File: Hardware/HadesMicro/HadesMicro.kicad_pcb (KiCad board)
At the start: 4 copper layers, 40 x 40 mm, 86 parts

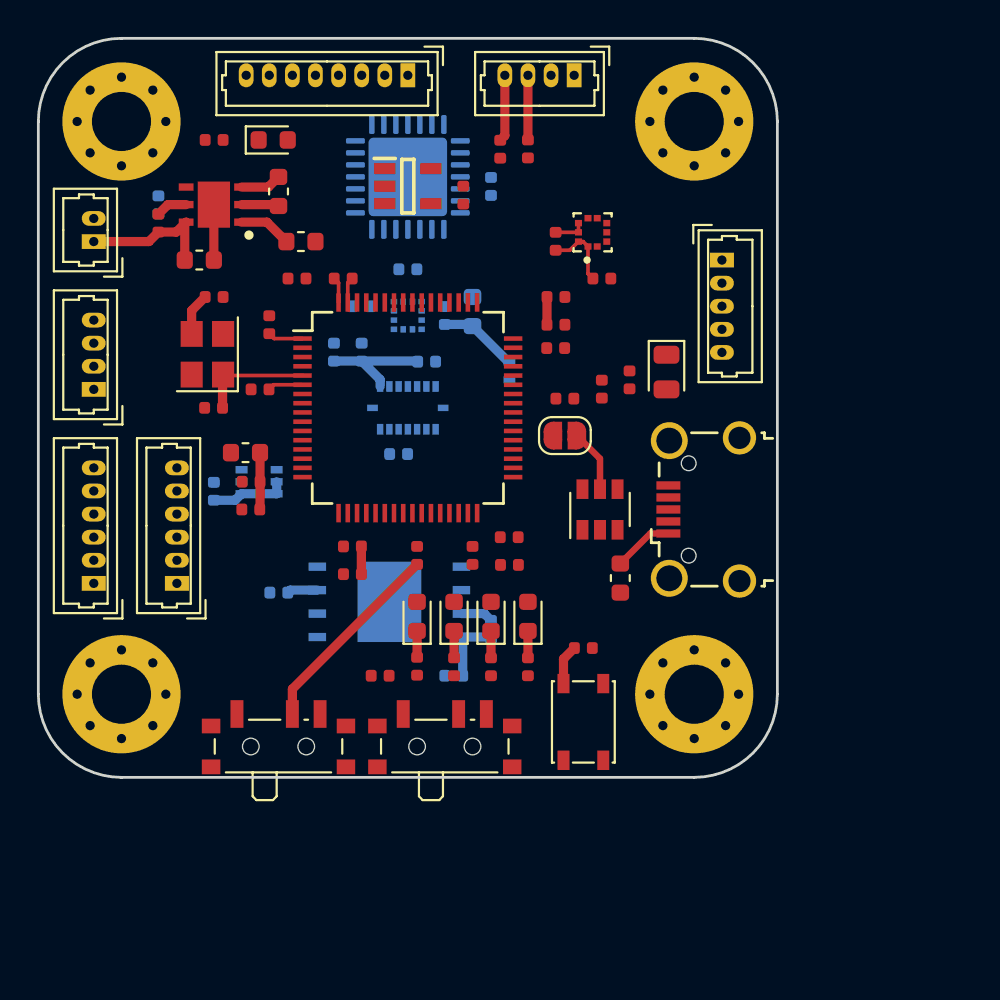
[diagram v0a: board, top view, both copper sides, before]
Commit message: Added TMP100 driver.
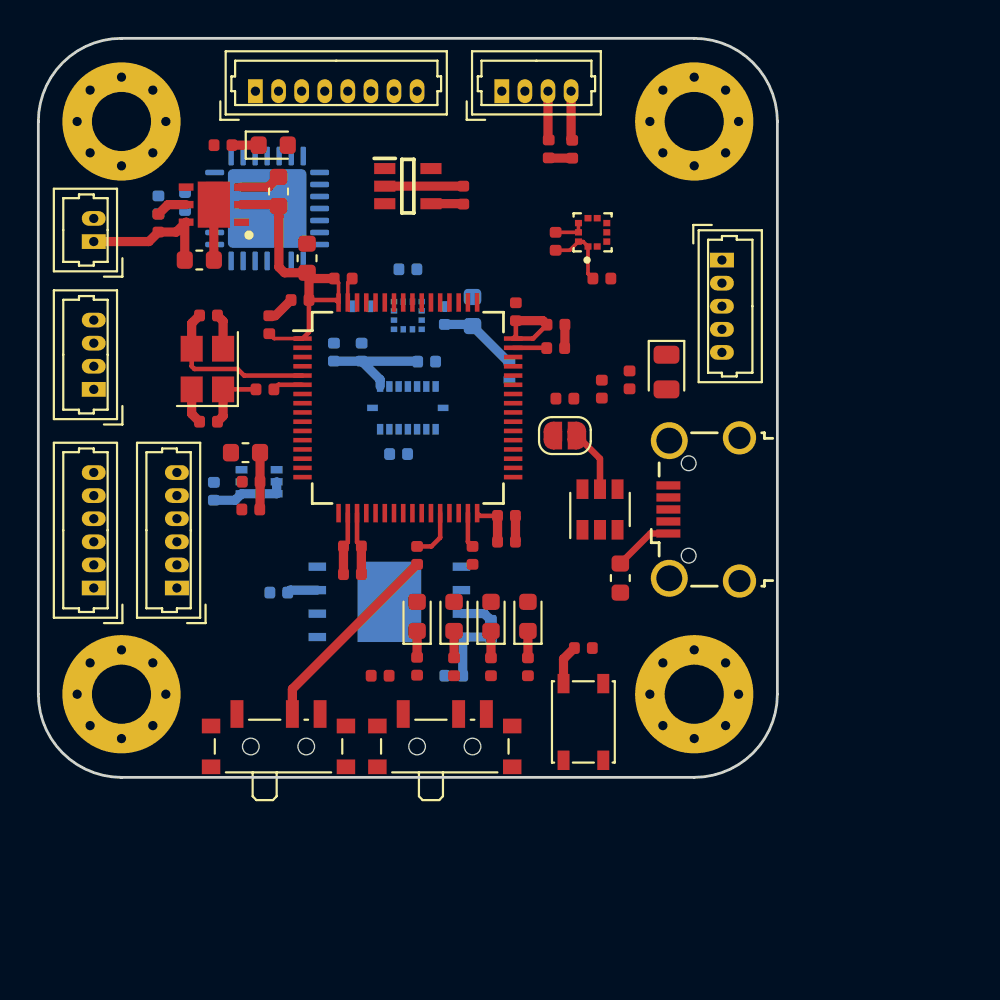
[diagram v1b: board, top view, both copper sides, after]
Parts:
- moved ? 16.6 mm to (27.9, 28.8), turned to 90 degrees
- moved ? 8.29 mm to (31.8, 22.9), turned to 0 degrees
- moved ? 7.80 mm to (32.4, 29.2), turned to 270 degrees
- moved ? 6.76 mm to (29.2, 40.8), turned to 180 degrees
- moved ? 5.01 mm to (29.2, 35.0), turned to 0 degrees
- moved ? 4.01 mm to (45.1, 22.9), turned to 0 degrees
- moved ? 3.90 mm to (48.9, 26.0)
- moved ? 2.31 mm to (45.8, 34.8), turned to 90 degrees
- moved ? 1.27 mm to (45.3, 47.2)
- moved ? 1.17 mm to (34.2, 34.2), turned to 180 degrees
- moved ? 1.16 mm to (45.3, 45.8)
- moved ? 1.12 mm to (47.6, 26.0)
- moved ? 0.96 mm to (34.5, 31.9), turned to 90 degrees
- moved ? 0.80 mm to (29.1, 37.9)
- moved ? 0.56 mm to (30.0, 25.8)
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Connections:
- ? pad 1: HSE_IN -> Net-(C18-Pad1)
- ? pad 3: Net-(C18-Pad1) -> HSE_IN
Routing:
- net +3V3: track 33.7 -> 54.1 mm
- net GND: track 8.36 -> 24.1 mm
- net HSE_IN: track 6.13 -> 9.13 mm
- net BOOT1: track 0.00 -> 2.77 mm
- net Net-(C13-Pad1): track 0.00 -> 1.90 mm
- net Net-(C14-Pad1): track 0.00 -> 1.82 mm
- net Net-(PWR1-Pad1): track 0.00 -> 1.45 mm
- net Net-(C18-Pad1): track 2.30 -> 3.68 mm
- net I2C3_SDA: track 3.62 -> 2.68 mm
- net I2C3_SCL: track 3.50 -> 2.66 mm

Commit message: Completed HadesMicro PCB. SWD works on F4.
- Finalised board. Added Gerbers and assembly files.
- Tested SWD via ST-LINK adapter and STM32F4 (NAVC). Debug works flawlessly in STM32CubeIDE.
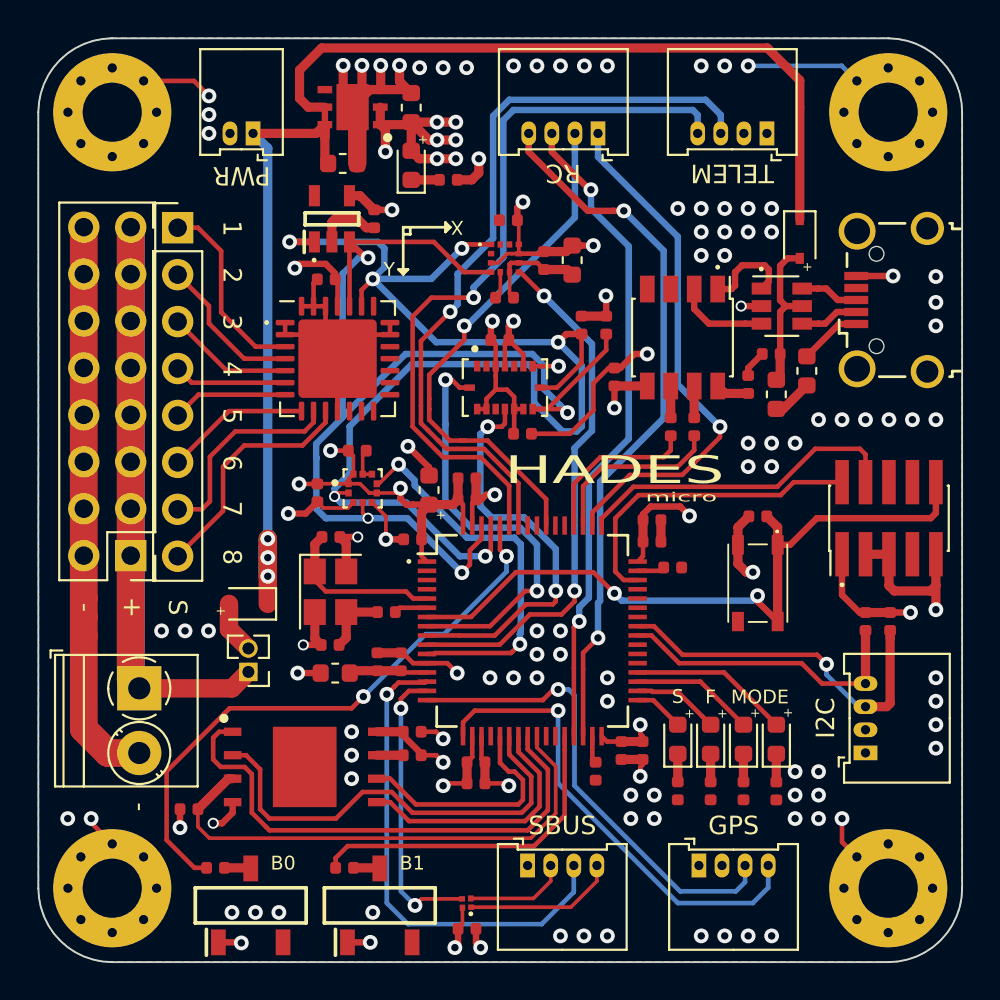
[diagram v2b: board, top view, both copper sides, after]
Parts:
- removed the ? at (55.5, 55.5)
- removed the ? at (37.0, 49.0)
- removed the ? at (37.0, 47.5)
- removed the ? at (45.3, 47.2)
- removed the ? at (45.3, 45.8)
- removed the ? at (48.0, 35.5)
- removed the ? at (45.8, 34.8)
- removed the ? at (32.5, 35.5)
- removed the ? at (36.5, 33.0)
- removed the ? at (43.5, 48.0)
- removed the ? at (48.0, 36.8)
- removed the ? at (24.5, 55.5)
- removed the ? at (31.5, 44.0)
- removed the ? at (31.5, 45.5)
- removed the ? at (29.2, 35.0)
- removed the ? at (29.2, 40.8)
- removed the ? at (43.0, 28.5)
- removed the ? at (41.0, 37.5)
- removed the ? at (39.5, 42.5)
- removed the ? at (40.0, 32.5)
- removed the ? at (37.5, 34.5)
- removed the ? at (42.0, 35.0)
- removed the ? at (24.5, 24.5)
- removed the ? at (43.5, 34.8)
- removed the ? at (50.5, 33.0)
- removed the ? at (48.0, 31.0)
- removed the ? at (27.9, 28.8)
- removed the ? at (49.5, 53.0)
- removed the ? at (42.5, 54.5)
- removed the ? at (29.5, 44.5)
- removed the ? at (40.5, 51.3)
- removed the ? at (42.5, 51.3)
- removed the ? at (44.5, 51.3)
- removed the ? at (46.5, 51.3)
- removed the ? at (54.0, 38.1)
- removed the ? at (31.2, 42.4)
- removed the ? at (51.5, 49.2)
- removed the ? at (45.1, 22.9)
- removed the ? at (31.9, 44.0)
- removed the ? at (48.5, 41.5)
- removed the ? at (31.8, 22.9)
- removed the ? at (32.7, 25.8)
- removed the ? at (26.5, 30.0)
- removed the ? at (26.5, 29.0)
- removed the ? at (30.0, 25.8)
- removed the ? at (37.5, 37.0)
- removed the ? at (28.7, 32.0)
- removed the ? at (36.0, 37.0)
- removed the ? at (47.6, 26.0)
- removed the ? at (48.9, 26.0)
- removed the ? at (32.3, 39.0)
- removed the ? at (40.5, 54.0)
- removed the ? at (42.5, 54.0)
- removed the ? at (44.5, 54.0)
- removed the ? at (46.5, 54.0)
- removed the ? at (52.0, 38.5)
- removed the ? at (50.5, 39.0)
- removed the ? at (33.0, 28.3)
- removed the ? at (48.5, 39.5)
- removed the ? at (45.5, 38.0)
- removed the ? at (38.5, 54.5)
- removed the ? at (40.5, 48.0)
- removed the ? at (44.5, 52.0)
- removed the ? at (33.0, 50.0)
- removed the ? at (23.0, 39.0)
- removed the ? at (42.0, 58.0)
- removed the ? at (33.0, 58.0)
- removed the ? at (34.5, 31.9)
- removed the ? at (49.5, 57.0)
- removed the ? at (57.0, 32.0)
- removed the ? at (23.0, 49.8)
- removed the ? at (27.5, 49.8)
- removed the ? at (23.0, 31.0)
- removed the ? at (55.5, 24.5)
- removed the ? at (34.2, 34.2)
- added ?: Conn_01x04, Connector_Molex:Molex_PicoBlade_53048-0810_1x04_P1.25mm_Horizontal, F.Cu at (50.3, 25.1)
- added ?: 10u, Capacitor_SMD:C_0603_1608Metric, F.Cu at (40.2, 23.7)
- added ?: 10u, Capacitor_SMD:C_0603_1608Metric, F.Cu at (41.1, 44.5)
- added ?: 100n, Capacitor_SMD:C_0402_1005Metric, F.Cu at (43.2, 45.0)
- added ?: 100n, Capacitor_SMD:C_0402_1005Metric, F.Cu at (43.2, 43.8)
- added ?: 100n, Capacitor_SMD:C_0402_1005Metric, F.Cu at (53.2, 47.2)
- added ?: 100n, Capacitor_SMD:C_0402_1005Metric, F.Cu at (53.2, 46.1)
- added ?: 100n, Capacitor_SMD:C_0402_1005Metric, F.Cu at (51.6, 58.5)
- added ?: 100n, Capacitor_SMD:C_0402_1005Metric, F.Cu at (52.7, 58.5)
- added ?: 100n, Capacitor_SMD:C_0402_1005Metric, F.Cu at (43.7, 59.2)
- added ?: 100n, Capacitor_SMD:C_0402_1005Metric, F.Cu at (43.7, 60.3)
- added ?: 100n, Capacitor_SMD:C_0402_1005Metric, F.Cu at (40.3, 47.1)
- added ?: 2u2, Capacitor_SMD:C_0402_1005Metric, F.Cu at (50.2, 59.7)
- added ?: 2u2, Capacitor_SMD:C_0402_1005Metric, F.Cu at (54.3, 48.6)
- added ?: 1u, Capacitor_SMD:C_0402_1005Metric, F.Cu at (39.6, 53.7)
- added ?: 100n, Capacitor_SMD:C_0402_1005Metric, F.Cu at (38.4, 53.7)
- added ?: 10p, Capacitor_SMD:C_0402_1005Metric, F.Cu at (35.8, 47.0)
- added ?: 10p, Capacitor_SMD:C_0402_1005Metric, F.Cu at (35.8, 52.8)
- added ?: 100n, Capacitor_SMD:C_0402_1005Metric, F.Cu at (38.2, 29.8)
- added ?: 100n, Capacitor_SMD:C_0402_1005Metric, F.Cu at (45.0, 36.3)
- added ?: 100n, Capacitor_SMD:C_0402_1005Metric, F.Cu at (46.2, 41.4)
- added ?: MountingHole_3.2mm_M3_Pad_Via, MountingHole:MountingHole_3.2mm_M3_Pad_Via, F.Cu at (24.0, 24.0)
- added ?: 220n, Capacitor_SMD:C_0402_1005Metric, F.Cu at (45.2, 34.0)
- added ?: 100n, Capacitor_SMD:C_0402_1005Metric, F.Cu at (45.4, 29.8)
- added ?: 100n, Capacitor_SMD:C_0402_1005Metric, F.Cu at (47.4, 32.0)
- added ?: 10u, Capacitor_SMD:C_0603_1608Metric, F.Cu at (48.9, 32.0)
- added ?: 100n, Capacitor_SMD:C_0402_1005Metric, F.Cu at (37.3, 42.3)
- added ?: 100n, Capacitor_SMD:C_0402_1005Metric, F.Cu at (35.1, 44.6)
- added ?: 100n, Capacitor_SMD:C_0402_1005Metric, F.Cu at (35.6, 33.0)
- added ?: 100n, Capacitor_SMD:C_0402_1005Metric, F.Cu at (58.9, 45.9)
- added ?: 100n, Capacitor_SMD:C_0402_1005Metric, F.Cu at (40.2, 57.5)
- added ?: 100n, Capacitor_SMD:C_0402_1005Metric, F.Cu at (43.2, 68.2)
- added ?: MountingHole_3.2mm_M3_Pad_Via, MountingHole:MountingHole_3.2mm_M3_Pad_Via, F.Cu at (66.0, 24.0)
- added ?: 100n, Capacitor_SMD:C_0402_1005Metric, F.Cu at (59.7, 37.1)
- added ?: 100n, Capacitor_SMD:C_0402_1005Metric, F.Cu at (58.4, 38.7)
- added ?: 100n, Capacitor_SMD:C_0402_1005Metric, F.Cu at (51.2, 38.3)
- added ?: GR, LED_SMD:LED_0603_1608Metric, F.Cu at (54.6, 57.9)
- added ?: RE, LED_SMD:LED_0603_1608Metric, F.Cu at (56.4, 57.9)
- added ?: YE, LED_SMD:LED_0603_1608Metric, F.Cu at (58.2, 57.9)
- added ?: BL, LED_SMD:LED_0603_1608Metric, F.Cu at (59.9, 57.9)
- added ?: D_Schottky, Diode_SMD:D_SOD-323, F.Cu at (61.2, 30.9)
- added ?: D_Schottky, Diode_SMD:D_SOD-323, F.Cu at (31.4, 50.6)
- added ?: MountingHole_3.2mm_M3_Pad_Via, MountingHole:MountingHole_3.2mm_M3_Pad_Via, F.Cu at (66.0, 66.0)
- added ?: Fuse, Fuse:Fuse_0603_1608Metric, F.Cu at (61.6, 38.0)
- added ?: FB_Small, Inductor_SMD:L_0603_1608Metric, F.Cu at (36.1, 54.4)
- added ?: FB_Small, Inductor_SMD:L_0603_1608Metric, F.Cu at (59.9, 39.3)
- added ?: , 74LVC1G04GX4Z:74AUP1G04GX4Z, F.Cu at (43.2, 66.8)
- added ?: Jumper_NO_Small, Connector_PinHeader_1.27mm:PinHeader_1x02_P1.27mm_Vertical, F.Cu at (31.4, 54.3)
- added ?: Conn_02x08_Odd_Even, Connector_PinHeader_2.54mm:PinHeader_2x08_P2.54mm_Vertical, F.Cu at (25.0, 48.0)
- added ?: Conn_01x08, Connector_PinHeader_2.54mm:PinHeader_1x08_P2.54mm_Vertical, F.Cu at (27.5, 30.3)
- added ?: GR, LED_SMD:LED_0603_1608Metric, F.Cu at (40.2, 26.9)
- added ?: 1k, Resistor_SMD:R_0402_1005Metric, F.Cu at (42.2, 27.7)
- added ?: 2k2, Resistor_SMD:R_0402_1005Metric, F.Cu at (49.4, 35.5)
- added ?: 2k2, Resistor_SMD:R_0402_1005Metric, F.Cu at (50.7, 35.5)
- added ?: 2k2, Resistor_SMD:R_0402_1005Metric, F.Cu at (66.1, 51.6)
- added ?: 2k2, Resistor_SMD:R_0402_1005Metric, F.Cu at (64.8, 51.6)
- added ?: 620, Resistor_SMD:R_0402_1005Metric, F.Cu at (38.8, 51.1)
- added ?: , TDD01H0SB1R:SOT175P420X230-3N, F.Cu at (31.5, 66.9)
- added ?: 1k, Resistor_SMD:R_0402_1005Metric, F.Cu at (54.6, 60.7)
- added ?: 1k, Resistor_SMD:R_0402_1005Metric, F.Cu at (56.4, 60.7)
- added ?: 1k, Resistor_SMD:R_0402_1005Metric, F.Cu at (58.2, 60.7)
- added ?: 2k2, Resistor_SMD:R_0402_1005Metric, F.Cu at (59.9, 60.7)
- added ?: 22, Resistor_SMD:R_0402_1005Metric, F.Cu at (55.5, 41.0)
- added ?: 22, Resistor_SMD:R_0402_1005Metric, F.Cu at (54.2, 41.0)
- added ?: 10k, Resistor_SMD:R_0402_1005Metric, F.Cu at (29.6, 64.9)
- added ?: 10k, Resistor_SMD:R_0402_1005Metric, F.Cu at (36.6, 64.9)
- added ?: 10k, Resistor_SMD:R_0402_1005Metric, F.Cu at (40.2, 58.8)
- added ?: 10k, Resistor_SMD:R_0402_1005Metric, F.Cu at (28.2, 61.7)
- added ?: , TDD01H0SB1R:SOT175P420X230-3N, F.Cu at (38.5, 66.9)
- added ?: , SKRPANE010:SKRPADE010, F.Cu at (58.9, 49.4)
- added ?: otter:CH330, Package_SO:SSOP-8_3.95x5.21x3.27mm_P1.27mm, F.Cu at (54.9, 36.2)
- added ?: MountingHole_3.2mm_M3_Pad_Via, MountingHole:MountingHole_3.2mm_M3_Pad_Via, F.Cu at (24.0, 66.0)
- added ?: TerminalBlock_Phoenix_PT-1,5-2-3.5-H_1x02_P3.50mm_Horizontal, TerminalBlock_Phoenix:TerminalBlock_Phoenix_PT-1,5-2-3.5-H_1x02_P3.50mm_Horizontal, F.Cu at (25.5, 55.2)
- added ?: 10u, Capacitor_SMD:C_0603_1608Metric, F.Cu at (36.5, 26.8)
- added GPS: Conn_01x04, Connector_Molex:Molex_PicoBlade_53048-0810_1x04_P1.25mm_Horizontal, F.Cu at (55.8, 64.8)
- added I2C: Conn_01x04, Connector_Molex:Molex_PicoBlade_53048-0810_1x04_P1.25mm_Horizontal, F.Cu at (64.8, 58.7)
- added PWR: Conn_01x02, Connector_Molex:Molex_PicoBlade_53048-0410_1x02_P1.25mm_Horizontal, F.Cu at (31.6, 25.1)
- added SBUS: Conn_01x04, Connector_Molex:Molex_PicoBlade_53048-0810_1x04_P1.25mm_Horizontal, F.Cu at (46.5, 64.8)
- added SWD: Conn_02x05_Counter_Clockwise, Connector_PinHeader_1.27mm:PinHeader_2x05_P1.27mm_Vertical_SMD, F.Cu at (66.0, 46.0)
- added TELEM: Conn_01x04, Connector_Molex:Molex_PicoBlade_53048-0810_1x04_P1.25mm_Horizontal, F.Cu at (59.4, 25.1)
- ? (x4): moved to F.Cu
- moved ? 18.6 mm to (37.6, 44.4), turned to 0 degrees
- moved ? 15.2 mm to (66.2, 34.2)
- moved ? 14.8 mm to (60.2, 34.5), turned to 0 degrees
- moved ? 13.8 mm to (46.7, 52.1)
- moved ? 13.8 mm to (35.8, 50.0), turned to 270 degrees
- moved ? 10.0 mm to (34.4, 59.4)
- moved ? 9.18 mm to (37.0, 23.7)
- moved ? 8.98 mm to (36.2, 37.3), turned to 0 degrees
- moved ? 6.10 mm to (45.3, 31.9)
- moved ? 5.37 mm to (45.3, 38.9)
- moved ? 4.47 mm to (35.9, 29.8), turned to 90 degrees
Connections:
- net Net-(U1-Pad6) renamed USB_CONN_D+
- ? pad 2: Net-(U1-Pad1) -> USB_CONN_D-
- ? pad 3: Net-(FLASH1-Pad3) -> FLASH_!WP
- ? pad 1: Net-(C18-Pad1) -> HSE_IN
- ? pad 3: HSE_IN -> Net-(C18-Pad1)
- ? pad 25: Net-(MCU1-Pad25) -> FLASH_!WP
- ? pad 42: USB_VBUS -> Net-(MCU1-Pad42)
- ? pad 43: USB_ID -> Net-(MCU1-Pad43)
- ? pad 44: USB_DM -> Net-(MCU1-Pad44)
- ? pad 45: USB_DP -> Net-(MCU1-Pad45)
- ? pad 5: Net-(R1-Pad1) -> VCC
- ? pad 1: Net-(U1-Pad1) -> USB_CONV_D+
- ? pad 3: Net-(R14-Pad2) -> USB_CONV_D-
- ? pad 4: Net-(R13-Pad2) -> USB_CONN_D-
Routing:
- net GND: track 24.1 -> 168.5 mm, vias 0 -> 105
- net I2C1_SCL: track 0.00 -> 72.9 mm, vias 0 -> 6
- net VCC: track 7.52 -> 74.8 mm, vias 0 -> 3
- net I2C1_SDA: track 0.00 -> 65.3 mm, vias 0 -> 4
- net Net-(JP1-Pad1): track 0.00 -> 56.6 mm
- net UART1_TX: track 0.00 -> 41.2 mm, vias 0 -> 1
- net +3V3: track 54.1 -> 94.7 mm, vias 0 -> 28
- net UART1_RX: track 0.00 -> 40.5 mm, vias 0 -> 1
- net TIM2_CH4: track 0.00 -> 38.6 mm, vias 0 -> 2
- net NRST: track 2.17 -> 38.4 mm, vias 0 -> 2
- net TIM2_CH3: track 0.00 -> 35.6 mm, vias 0 -> 2
- net BOOT0: track 0.00 -> 32.0 mm, vias 0 -> 2
- net INT_MAG: track 0.00 -> 28.9 mm, vias 0 -> 2
- net TIM2_CH1: track 0.00 -> 28.5 mm, vias 0 -> 1
- net TIM2_CH2: track 0.00 -> 28.4 mm, vias 0 -> 1
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- added copper zone on In2.Cu, net +3V3
- added copper zone on B.Cu, net GND
- added copper zone on F.Cu, net GND
- added copper zone on In1.Cu, net GND
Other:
- board size 40 x 40 mm -> 50 x 50 mm
- net class Default: clearance 0.2 -> 0.15
- rule pad_to_mask_clearance: 0.2 -> 0
- rule trace_clearance: 0.2 -> 0.15
- board text added: "+"
- board text added: "-"
- board text added: "1"
- board text added: "12/19"
- board text added: "2"
- board text added: "3"
- board text added: "3V3"
- board text added: "4"
- board text added: "5"
- board text added: "6"
- board text added: "7"
- board text added: "8"
- board text added: "B0"
- board text added: "B1"
- board text added: "BAR1"
- board text added: "BOOT0"
- board text added: "BOOT1"
- board text added: "C1"
- board text added: "C10"
- board text added: "C11"
- board text added: "C12"
- board text added: "C13"
- board text added: "C14"
- board text added: "C15"
- board text added: "C16"
- board text added: "C17"
- board text added: "C18"
- board text added: "C19"
- board text added: "C2"
- board text added: "C20"
- board text added: "C21"
- board text added: "C22"
- board text added: "C23"
- board text added: "C24"
- board text added: "C25"
- board text added: "C26"
- board text added: "C27"
- board text added: "C28"
- board text added: "C29"
- board text added: "C3"
- board text added: "C30"
- board text added: "C31"
- board text added: "C32"
- board text added: "C33"
- board text added: "C34"
- board text added: "C4"
- board text added: "C5"
- board text added: "C6"
- board text added: "C7"
- board text added: "C8"
- board text added: "C9"
- board text added: "CH1"
- board text added: "CH2"
- board text added: "CH3"
- board text added: "CH4"
- board text added: "D1"
- board text added: "D2"
- board text added: "D3"
- board text added: "D4"
- board text added: "D5"
- board text added: "D6"
- board text added: "EEPROM1"
- board text added: "F"
- board text added: "F1"
- board text added: "FB1"
- board text added: "FB2"
- board text added: "FLASH1"
- board text added: "GND"
- board text added: "GPS1"
- board text added: "HADES"
- board text added: "HSE1"
- board text added: "I2C3"
- board text added: "IC1"
- board text added: "IMU1"
- board text added: "JP1"
- board text added: "M"
- board text added: "MAG1"
- board text added: "MCU1"
- board text added: "MODE"
- board text added: "P"
- board text added: "PWM1"
- board text added: "PWM_PWR1"
- board text added: "PWR"
- board text added: "PWR1"
- board text added: "R10"
- board text added: "R11"
- board text added: "R12"
- board text added: "R13"
- board text added: "R14"
- board text added: "R17"
- board text added: "R18"
- board text added: "R19"
- board text added: "R20"
- board text added: "R3"
- board text added: "R4"
- board text added: "R5"
- board text added: "R6"
- board text added: "R7"
- board text added: "R8"
- board text added: "R9"
- board text added: "RC"
- board text added: "RC1"
- board text added: "REG1"
- board text added: "RESET1"
- board text added: "RX"
- board text added: "S"
- board text added: "SBUS1"
- board text added: "SCL"
- board text added: "SDA"
- board text added: "SERVO1"
- board text added: "SWD1"
- board text added: "TELEM1"
- board text added: "TX"
- board text added: "U1"
- board text added: "U2"
- board text added: "USB1"
- board text added: "VIN1"
- board text added: "X"
- board text added: "Y"
- board text added: "micro"
- board text added: "philsal.co.uk"
